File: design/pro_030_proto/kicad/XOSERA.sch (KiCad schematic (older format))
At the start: 38 parts, among them IC16 74LS74, IC17 74HCT245, IC18 74HCT245, IC19 74HCT245, J10 Upduino_LHS, J11 Upduino_RHS, J12 Conn_01x06_Male, J13 PMOD_TOP, J14 PMOD_BOTTOM, J15 Conn_02x04_Counter_Clockwise, J16 Conn_02x04_Counter_Clockwise, Q1 2N3904

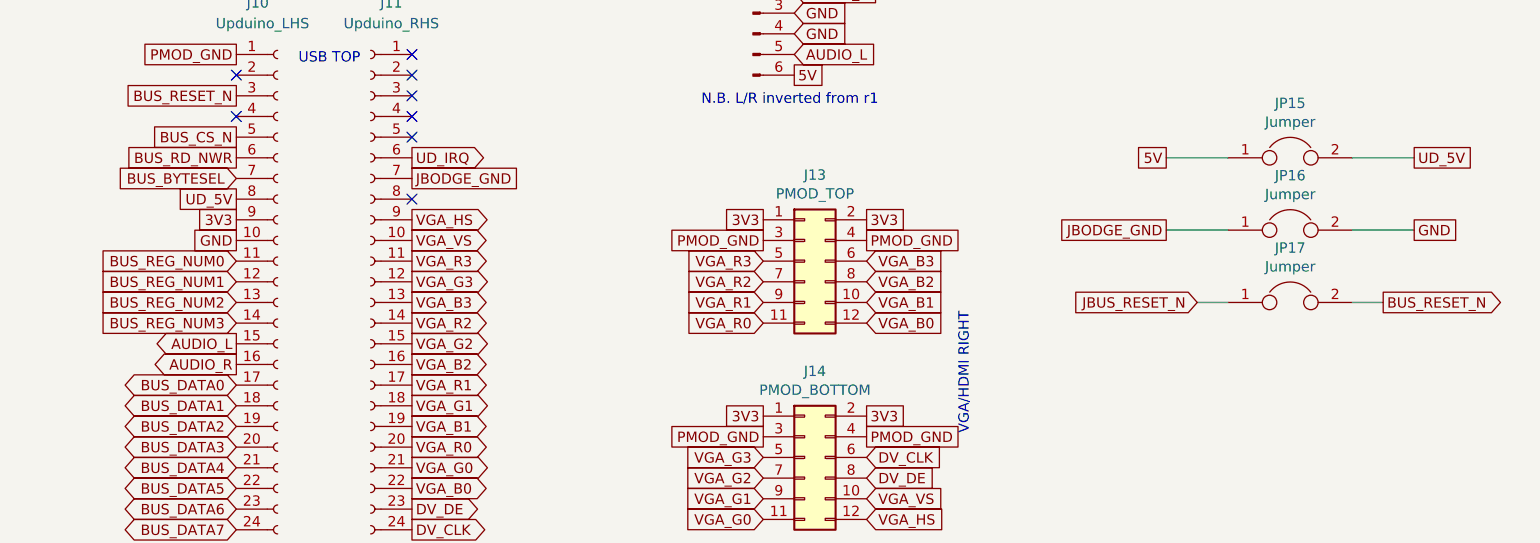
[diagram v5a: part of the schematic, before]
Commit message: Lots more changes
* Add DIN expansion connectors (provisional pinout)
* Fix incorrect address lines for RAM & ROM (Doh!)
* Remove unused level shifters
* Fix clock enables
* Lots of other small fixes
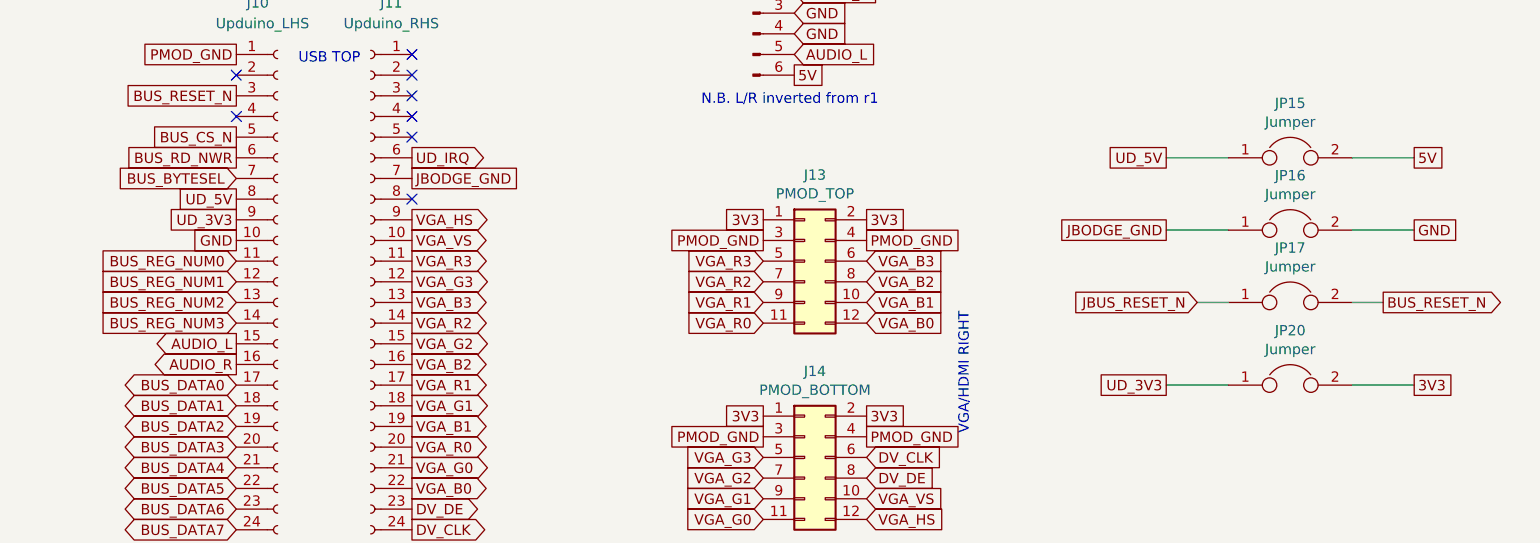
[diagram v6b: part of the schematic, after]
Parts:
- added JP20: Jumper, Connector_PinHeader_2.54mm:PinHeader_1x02_P2.54mm_Vertical, symbol Device:Jumper
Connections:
- net 3V3: now also JP20.2; no longer J10.9 (Pin_9)
- net 5V: now also JP15.2; no longer JP15.1
- net UD_5V: now also JP15.1; no longer JP15.2
- new net UD_3V3: J10.9 (Pin_9), JP20.1
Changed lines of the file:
@@
 $Descr A4 11693 8268
 encoding utf-8
-Sheet 11 15
+Sheet 11 14
 Title "rosco_m68k Pro (030) Prototype"
 Date "2021-10-01"
@@
 Wire Wire Line
 	9900 1650 9600 1650
+Text GLabel 9600 1650 0    50   UnSpc ~ 0
+UD_5V
 Text GLabel 10800 1650 2    50   UnSpc ~ 0
-UD_5V
-Text GLabel 9600 1650 0    50   UnSpc ~ 0
 5V
 $Comp
@@
 UD_5V
 Text GLabel 5100 1950 0    50   UnSpc ~ 0
-3V3
+UD_3V3
 Text GLabel 5100 2050 0    50   UnSpc ~ 0
 GND
@@
 Text Notes 7350 1400 0    50   ~ 0
 N.B. L/R inverted from r1
+$Comp
+L Device:Jumper JP20
+U 1 1 619B1631
+P 10200 2750
+F 0 "JP20" H 10200 3014 50  0000 C CNN
+F 1 "Jumper" H 10200 2923 50  0000 C CNN
+F 2 "Connector_PinHeader_2.54mm:PinHeader_1x02_P2.54mm_Vertical" H 10200 2750 50  0001 C CNN
+F 3 "~" H 10200 2750 50  0001 C CNN
+	1    10200 2750
+	1    0    0    -1
+$EndComp
+Wire Wire Line
+	9900 2750 9600 2750
+Text GLabel 9600 2750 0    50   UnSpc ~ 0
+UD_3V3
+Text GLabel 10800 2750 2    50   UnSpc ~ 0
+3V3
+Wire Wire Line
+	10500 2750 10800 2750
 $EndSCHEMATC

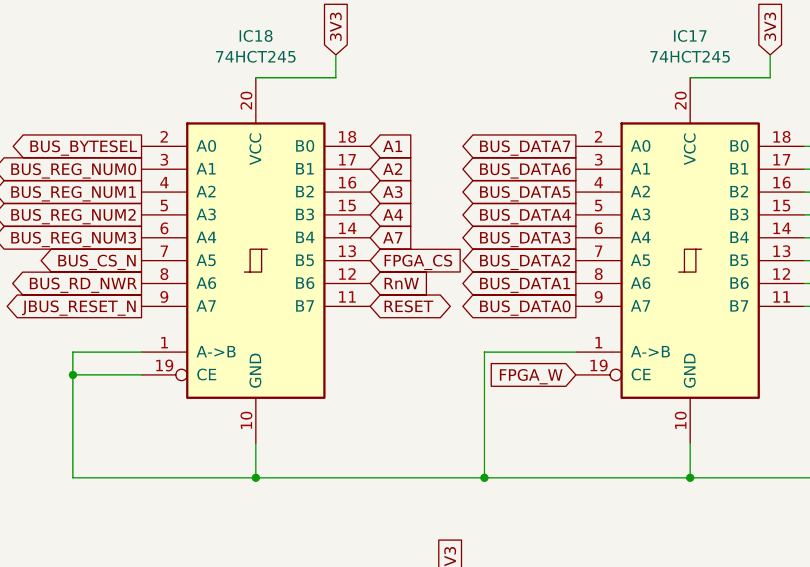
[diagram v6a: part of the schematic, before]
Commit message: Fix RW/RnW SNAFU
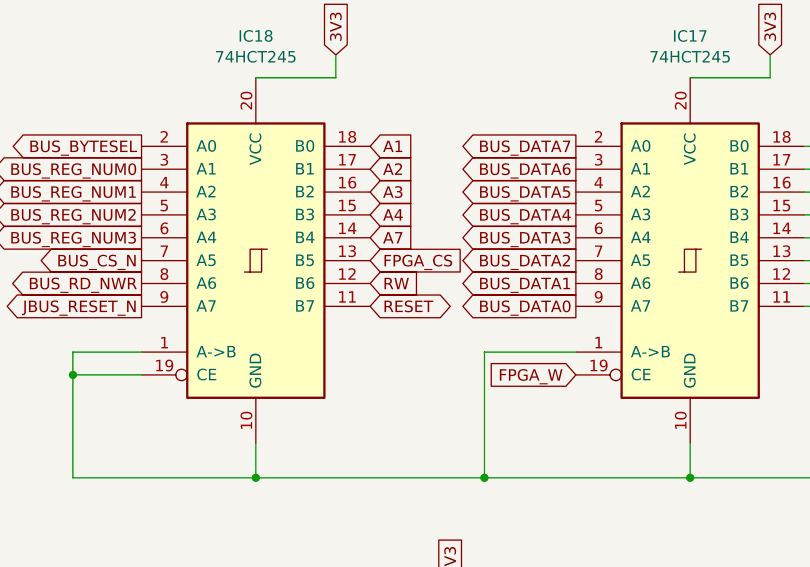
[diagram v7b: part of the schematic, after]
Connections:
- net RnW renamed RW
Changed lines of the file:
@@
 BUS_CS_N
 Text GLabel 3800 5200 2    50   Input ~ 0
-RnW
+RW
 Text GLabel 2800 5200 0    50   Output ~ 0
 BUS_RD_NWR

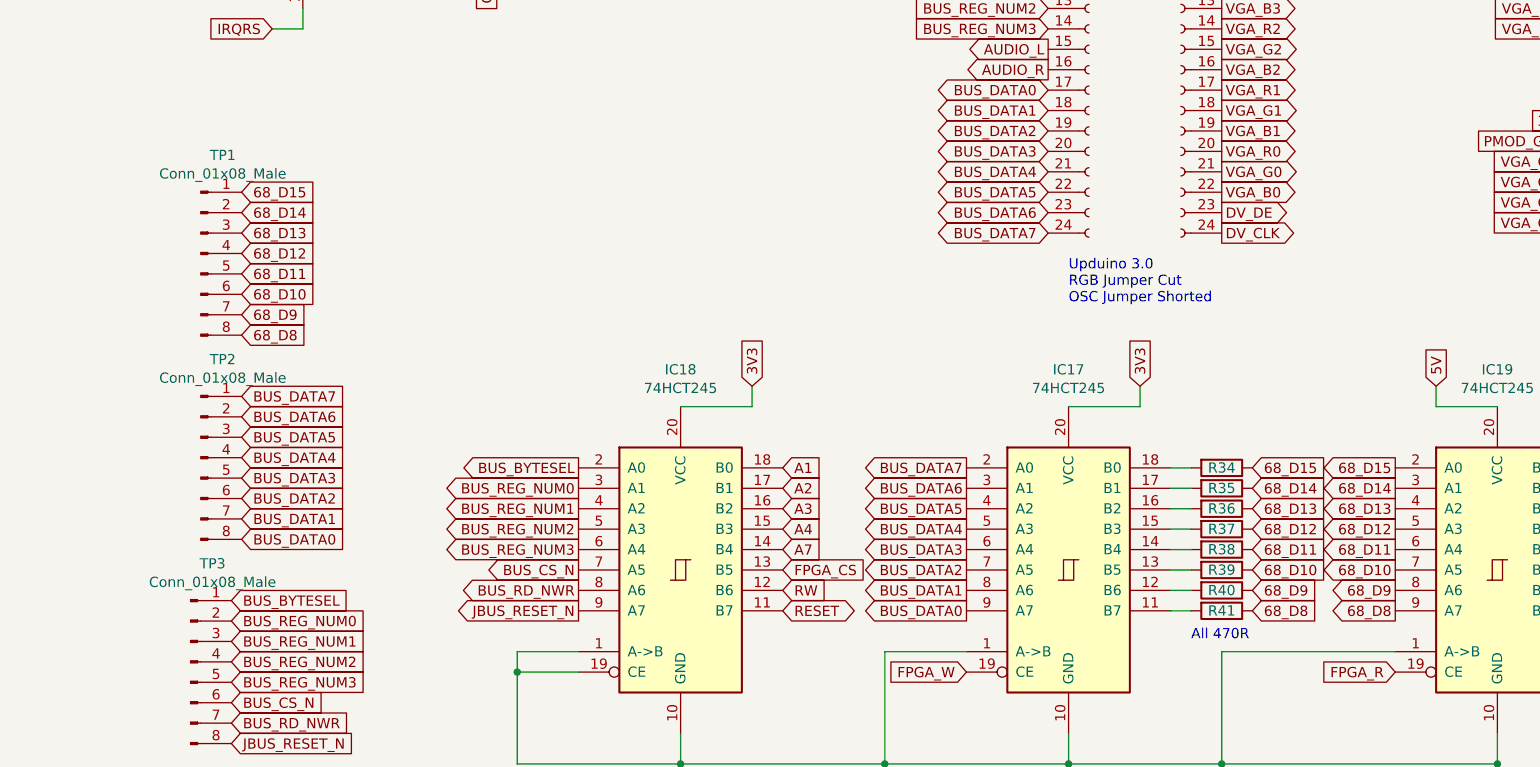
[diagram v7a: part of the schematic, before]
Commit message: Fix (another) hilarious mistake 😞
* 8-bit ports wired to the wrong end of the bus
* Another respin needed I think...
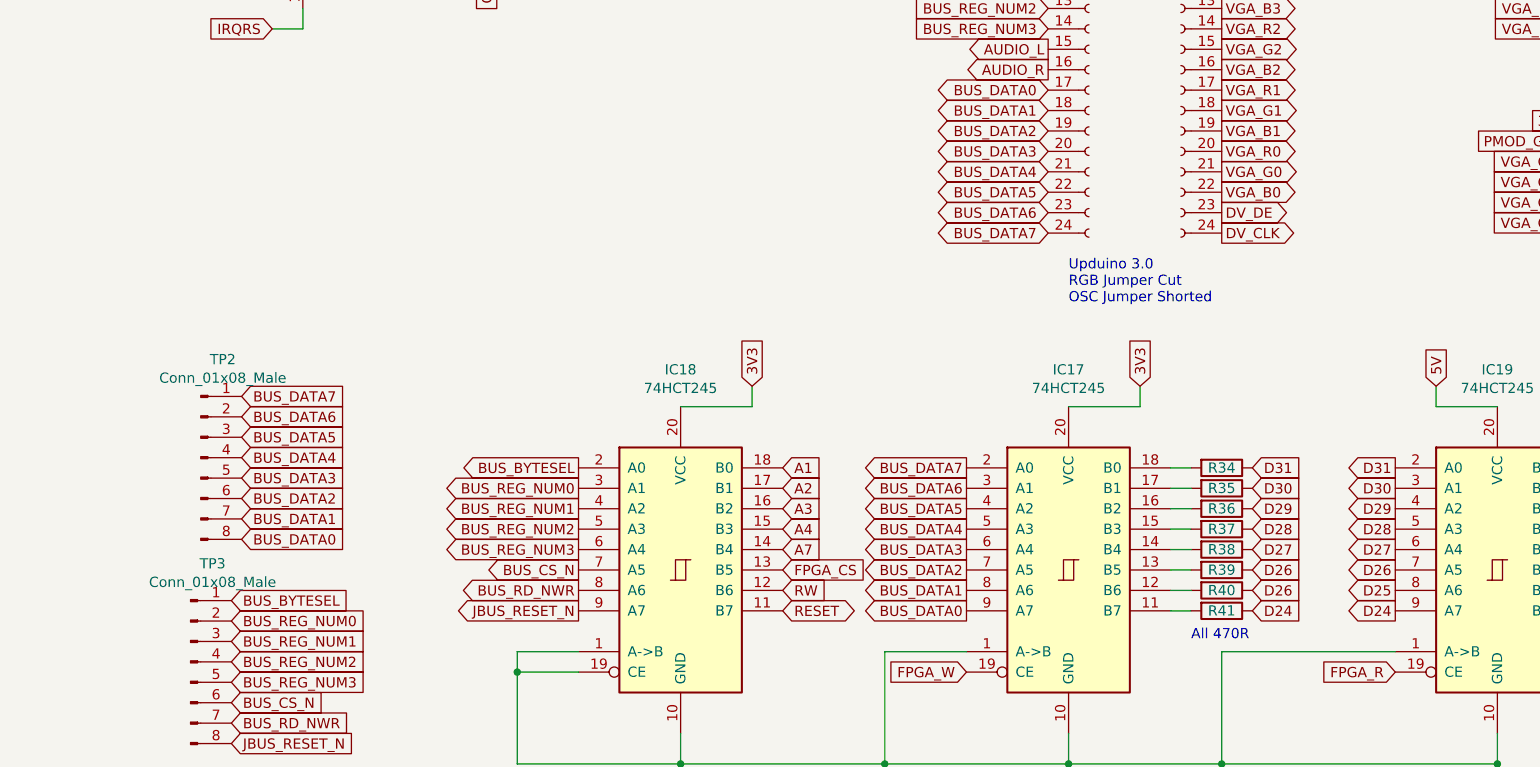
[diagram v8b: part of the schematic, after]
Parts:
- removed TP1: Conn_01x08_Male, Connector_PinHeader_2.54mm:PinHeader_1x08_P2.54mm_Vertical, symbol Connector:Conn_01x08_Male
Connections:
- net 68_D10 renamed D26
- net D26: now also R40.1
- net 68_D11 renamed D27
- net 68_D12 renamed D28
- net 68_D13 renamed D29
- net 68_D14 renamed D30
- net 68_D15 renamed D31
- net 68_D8 renamed D24
- net 68_D9 renamed D25
- net D25: no longer R40.1
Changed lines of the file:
@@
 	5700 5300 5800 5300
 Text GLabel 6100 5300 2    50   Input ~ 0
-68_D8
+D24
 Text GLabel 6100 5200 2    50   Input ~ 0
-68_D9
+D26
 Text GLabel 6100 5100 2    50   Input ~ 0
-68_D10
+D26
 Text GLabel 6100 5000 2    50   Input ~ 0
-68_D11
+D27
 Text GLabel 6100 4900 2    50   Input ~ 0
-68_D12
+D28
 Text GLabel 6100 4800 2    50   Input ~ 0
-68_D13
+D29
 Text GLabel 6100 4700 2    50   Input ~ 0
-68_D14
+D30
 Text GLabel 6100 4600 2    50   Input ~ 0
-68_D15
+D31
 Text GLabel 6800 5300 0    50   Output ~ 0
-68_D8
+D24
 Text GLabel 6800 5200 0    50   Output ~ 0
-68_D9
+D25
 Text GLabel 6800 5100 0    50   Output ~ 0
-68_D10
+D26
 Text GLabel 6800 5000 0    50   Output ~ 0
-68_D11
+D27
 Text GLabel 6800 4900 0    50   Output ~ 0
-68_D12
+D28
 Text GLabel 6800 4800 0    50   Output ~ 0
-68_D13
+D29
 Text GLabel 6800 4700 0    50   Output ~ 0
-68_D14
+D30
 Text GLabel 6800 4600 0    50   Output ~ 0
-68_D15
+D31
 Text GLabel 7800 5300 2    50   Input ~ 0
 BUS_DATA0
@@
 All BUS_xxx signals are 3V3\nUpduino-compatible signals
 $Comp
-L Connector:Conn_01x08_Male TP1
-U 1 1 60633B4A
-P 950 3550
-F 0 "TP1" H 1058 4031 50  0000 C CNN
-F 1 "Conn_01x08_Male" H 1058 3940 50  0000 C CNN
-F 2 "Connector_PinHeader_2.54mm:PinHeader_1x08_P2.54mm_Vertical" H 950 3550 50  0001 C CNN
-F 3 "~" H 950 3550 50  0001 C CNN
-	1    950  3550
-	1    0    0    -1
-$EndComp
-$Comp
 L Connector:Conn_01x08_Male TP2
 U 1 1 6063609C
@@
 	1    0    0    -1
 $EndComp
-Text GLabel 1150 3950 2    50   Input ~ 0
-68_D8
-Text GLabel 1150 3850 2    50   Input ~ 0
-68_D9
-Text GLabel 1150 3750 2    50   Input ~ 0
-68_D10
-Text GLabel 1150 3650 2    50   Input ~ 0
-68_D11
-Text GLabel 1150 3550 2    50   Input ~ 0
-68_D12
-Text GLabel 1150 3450 2    50   Input ~ 0
-68_D13
-Text GLabel 1150 3350 2    50   Input ~ 0
-68_D14
-Text GLabel 1150 3250 2    50   Input ~ 0
-68_D15
 Text GLabel 1150 4250 2    50   Input ~ 0
 BUS_DATA7
